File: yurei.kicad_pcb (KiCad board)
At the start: 2 copper layers, 345 x 122 mm, 179 parts, among them SW1 SW_SPST, SW10 SW_SPST, SW11 SW_SPST, SW12 SW_SPST, SW13 SW_SPST, SW14 SW_SPST, SW15 SW_SPST, SW16 SW_SPST, SW17 SW_SPST, SW18 SW_SPST, SW19 SW_SPST, SW2 SW_SPST, SW20 SW_SPST, SW21 SW_SPST, SW22 SW_SPST, SW23 SW_SPST, SW24 SW_SPST, SW25 SW_SPST, SW26 SW_SPST, SW27 SW_SPST, SW28 SW_SPST, SW29 SW_SPST, SW3 SW_SPST, SW30 SW_SPST, SW31 SW_SPST, SW32 SW_SPST, SW33 SW_SPST, SW34 SW_SPST, SW35 SW_SPST, SW36 SW_SPST, SW37 SW_SPST, SW38 SW_SPST, SW39 SW_SPST, SW4 SW_SPST, SW40 SW_SPST, SW41 SW_SPST, SW42 SW_SPST, SW43 SW_SPST, SW44 SW_SPST, SW45 SW_SPST, SW46 SW_SPST, SW47 SW_SPST, SW48 SW_SPST, SW49 SW_SPST, SW5 SW_SPST, SW50 SW_SPST, SW51 SW_SPST, SW52 SW_SPST, SW53 SW_SPST, SW54 SW_SPST, SW55 SW_SPST, SW56 SW_SPST, SW57 SW_SPST, SW58 SW_SPST, SW59 SW_SPST, SW6 SW_SPST, SW60 SW_SPST, SW61 SW_SPST, SW62 SW_SPST, SW63 SW_SPST, SW64 SW_SPST, SW65 SW_SPST, SW66 SW_SPST, SW67 SW_SPST, SW68 SW_SPST, SW69 SW_SPST, SW7 SW_SPST, SW70 SW_SPST, SW71 SW_SPST, SW72 SW_SPST, SW73 SW_SPST, SW74 SW_SPST, SW75 SW_SPST, SW76 SW_SPST, SW77 SW_SPST, SW78 SW_SPST, SW79 SW_SPST, SW8 SW_SPST, SW80 SW_SPST, SW81 SW_SPST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

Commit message: Routed
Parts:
- moved D85 20.9 mm to (326.6, 170.9)
- moved D4 19.5 mm to (111.9, 85.7)
- moved U1 18.8 mm to (131.0, 93.7)
- moved R1 3.27 mm to (332.3, 91.5)
- moved R2 3.27 mm to (351.3, 91.5)
- moved D70 2.46 mm to (193.2, 170.9)
- moved L2 2.03 mm to (363.4, 96.0)
- moved D53 1.89 mm to (107.5, 151.8)
- moved D54 1.89 mm to (126.5, 151.8)
- moved D55 1.89 mm to (145.6, 151.8)
- moved D56 1.89 mm to (164.6, 151.8)
- moved D57 1.89 mm to (183.7, 151.8)
- moved D58 1.89 mm to (202.7, 151.8)
- moved D59 1.89 mm to (221.8, 151.8)
- moved D60 1.89 mm to (240.8, 151.8)
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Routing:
- net Row5: track 0.00 -> 418.6 mm
- net Row4: track 0.00 -> 372.6 mm
- net Col16: track 0.00 -> 362.0 mm
- net Col15: track 0.00 -> 341.8 mm
- net Row1: track 0.00 -> 341.1 mm
- net Row2: track 0.00 -> 338.8 mm
- net Col14: track 0.00 -> 318.1 mm
- net Row0: track 0.00 -> 311.5 mm
- net Col12: track 0.00 -> 304.9 mm, vias 0 -> 1
- net Row3: track 0.00 -> 301.6 mm
- net Col13: track 0.00 -> 291.3 mm
- net Col11: track 0.00 -> 271.6 mm, vias 0 -> 1
- net Col10: track 0.00 -> 247.5 mm, vias 0 -> 1
- net Col9: track 0.00 -> 233.5 mm
- net LED2: track 0.00 -> 226.0 mm, vias 0 -> 1
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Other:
- outline, holes or cut-outs redrawn

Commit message: Create gerber files
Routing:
- added copper zone on B.Cu, net GND
- added copper zone on F.Cu, net GND
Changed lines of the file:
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@@
     (pcbplotparams
       (layerselection 0x010fc_ffffffff)
-      (usegerberextensions false)
+      (usegerberextensions true)
       (usegerberattributes false)
       (usegerberadvancedattributes false)
@@
       (outputformat 1)
       (mirror false)
-      (drillshape 1)
+      (drillshape 0)
       (scaleselection 1)
-      (outputdirectory ""))
+      (outputdirectory "gerber/"))
   )
   (net 0 "")
@@
   (segment (start 305.121 104.848) (end 309.884 109.611) (width 0.25) (layer B.Cu) (net 115))
   (segment (start 309.884 109.611) (end 309.884 123.898) (width 0.25) (layer B.Cu) (net 115))
+  (zone (net 95) (net_name GND) (layer F.Cu) (hatch edge 0.508)
+    (connect_pads (clearance 0.508))
+    (min_thickness 0.254)
+    (fill yes (arc_segments 32) (thermal_gap 0.508) (thermal_bridge_width 0.508))
+    (polygon
+      (pts
+        (xy 34.8 71.1) (xy 34.8 197.2) (xy 384.8 197.2) (xy 384.8 71.7)
+      )
+    )
+  )
+  (zone (net 95) (net_name GND) (layer B.Cu) (hatch edge 0.508)
+    (connect_pads (clearance 0.508))
+    (min_thickness 0.254)
+    (fill yes (arc_segments 32) (thermal_gap 0.508) (thermal_bridge_width 0.508))
+    (polygon
+      (pts
+        (xy 34.7 71.1) (xy 34.7 197.3) (xy 384.9 197.3) (xy 384.9 71.7)
+      )
+    )
+  )
 )

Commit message: Clean up
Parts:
- U1: footprint teensy:Teensy2.0 -> yurei:Teensy2.0
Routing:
- net Row5: track 418.6 -> 0.00 mm
- net Row4: track 372.6 -> 0.00 mm
- net Col16: track 362.0 -> 0.00 mm
- net Col15: track 341.8 -> 0.00 mm
- net Row1: track 341.1 -> 0.00 mm
- net Row2: track 338.8 -> 0.00 mm
- net Col14: track 318.1 -> 0.00 mm
- net Row0: track 311.5 -> 0.00 mm
- net Col12: track 304.9 -> 0.00 mm, vias 1 -> 0
- net Row3: track 301.6 -> 0.00 mm
- net Col13: track 291.3 -> 0.00 mm
- net Col11: track 271.6 -> 0.00 mm, vias 1 -> 0
- net Col10: track 247.5 -> 0.00 mm, vias 1 -> 0
- net Col9: track 233.5 -> 0.00 mm
- net LED2: track 226.0 -> 0.00 mm, vias 1 -> 0
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- removed copper zone on B.Cu, net GND
- removed copper zone on F.Cu, net GND

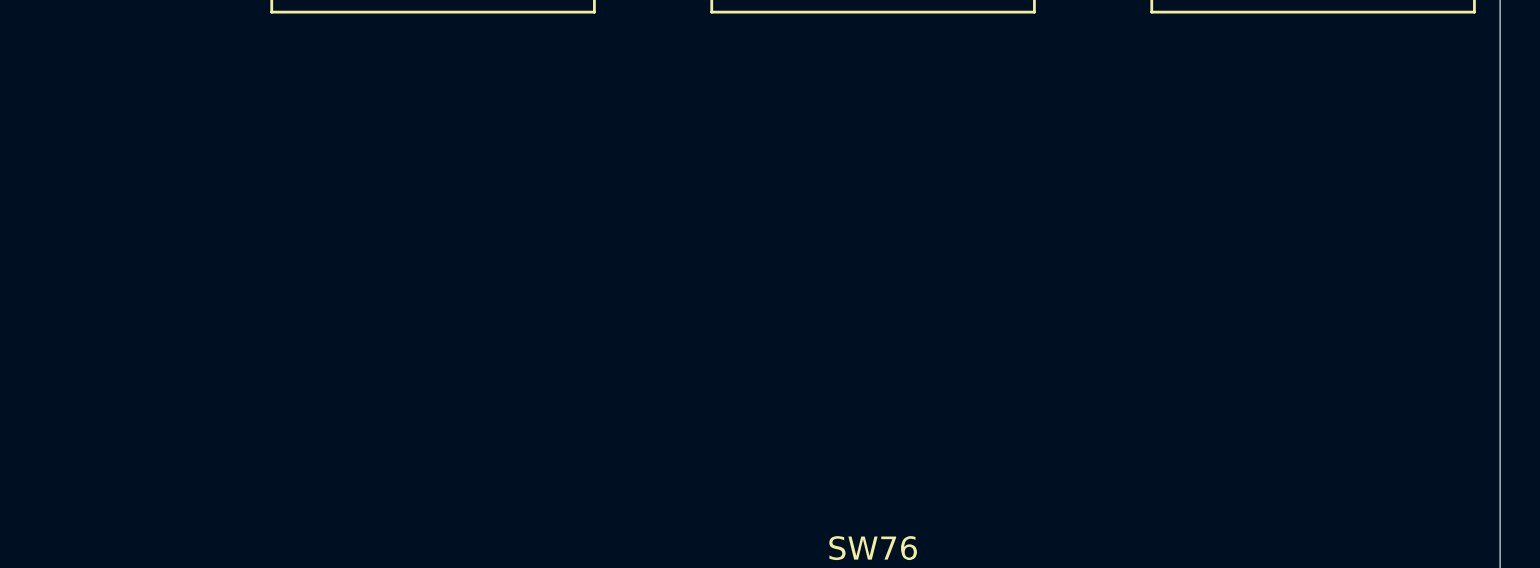
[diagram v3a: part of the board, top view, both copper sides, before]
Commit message: Add logo to PCB
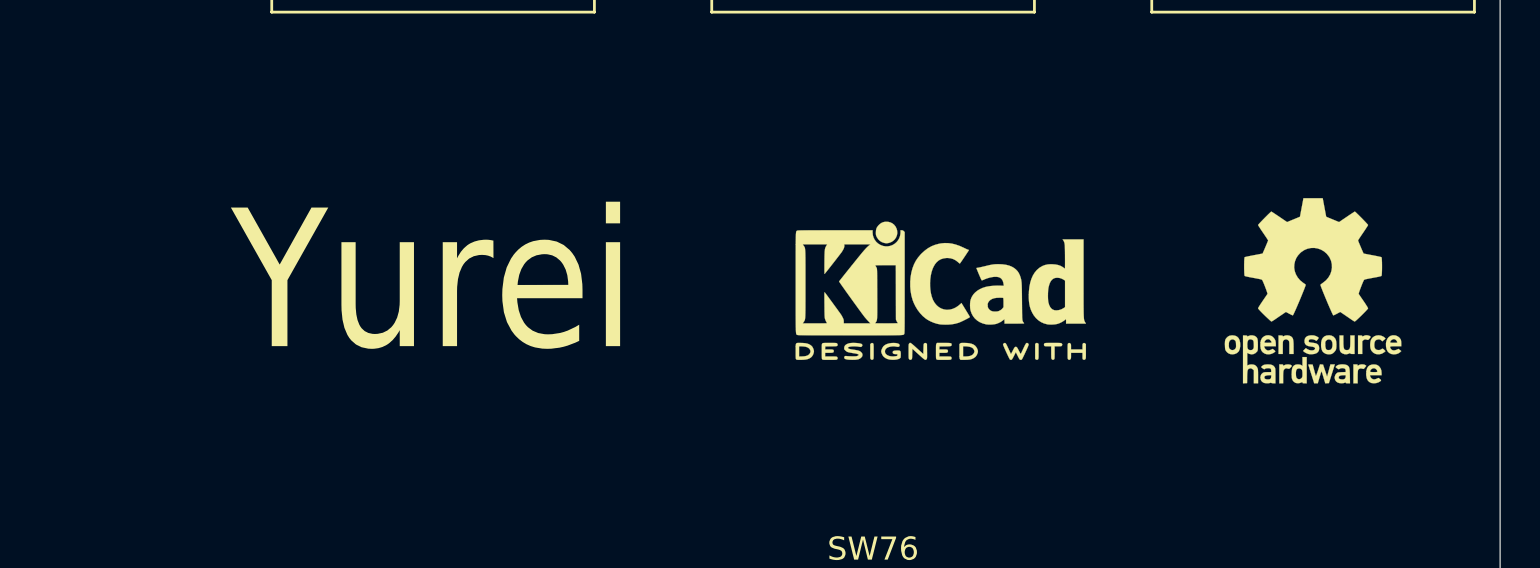
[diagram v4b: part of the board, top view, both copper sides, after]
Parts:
- added REF**: KiCad-Logo2_5mm_SilkScreen, Symbol:KiCad-Logo2_5mm_SilkScreen, B.Cu at (346.4, 148.0)
- added REF**: OSHW-Logo_7.5x8mm_SilkScreen, Symbol:OSHW-Logo_7.5x8mm_SilkScreen, B.Cu at (330.2, 148.0)
- added REF**: OSHW-Logo_7.5x8mm_SilkScreen, Symbol:OSHW-Logo_7.5x8mm_SilkScreen, F.Cu at (374.2, 148.0)
- added REF**: KiCad-Logo2_5mm_SilkScreen, Symbol:KiCad-Logo2_5mm_SilkScreen, F.Cu at (358.1, 148.0)
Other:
- board text added: "Yurei"

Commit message: Update footprint
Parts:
- REF** (x2): footprint Symbol:OSHW-Logo_7.5x8mm_SilkScreen -> yurei:OSHW-Logo_7.5x8mm_SilkScreen
- REF** (x2): footprint Symbol:KiCad-Logo2_5mm_SilkScreen -> yurei:KiCad-Logo2_5mm_SilkScreen

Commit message: Update footprints
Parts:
- moved REF** 2.95 mm to (349.3, 148.0)
- moved REF** 1.98 mm to (332.2, 148.0)
- moved REF** 0.98 mm to (357.1, 148.0)

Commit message: Update route
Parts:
- renumbered REF** to kicad1, REF** to kicad2, REF** to oshw1, REF** to oshw2
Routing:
- net Row5: track 0.00 -> 419.3 mm
- net Row4: track 0.00 -> 378.7 mm
- net Col16: track 0.00 -> 362.5 mm
- net Row1: track 0.00 -> 341.3 mm
- net Col15: track 0.00 -> 341.2 mm
- net Row2: track 0.00 -> 338.8 mm
- net Col12: track 0.00 -> 320.7 mm
- net Col14: track 0.00 -> 318.3 mm
- net Row0: track 0.00 -> 312.6 mm
- net Row3: track 0.00 -> 303.3 mm
- net Col13: track 0.00 -> 283.2 mm, vias 0 -> 1
- net Col11: track 0.00 -> 268.5 mm, vias 0 -> 1
- net Col10: track 0.00 -> 251.4 mm, vias 0 -> 1
- net LED2: track 0.00 -> 223.9 mm
- net GND: track 0.00 -> 222.3 mm
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- added copper zone on B.Cu, net GND
- added copper zone on F.Cu, net GND
